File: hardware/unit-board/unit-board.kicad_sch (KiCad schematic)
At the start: 0 parts

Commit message: Add unit board schematic blocks
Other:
- added sheet CAN Interface (can_interface.kicad_sch)
- added sheet G474 Minimum (STM32G474 Minimum System.kicad_sch)
- added sheet Power Input 3.3V (power_3v3.kicad_sch)
- added sheet Power monitoring (5V monitoring.kicad_sch)
- added sheet SPI,LED,CAN_ID (amt22_spi.kicad_sch)
- title: (none) -> unit bozrd
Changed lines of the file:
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@@
 	(generator_version "10.0")
 	(paper "A4")
+	(title_block
+		(title "unit bozrd")
+		(date "2026-07-21")
+	)
+	(sheet
+		(at 142.24 21.59)
+		(size 48.26 48.26)
+		(exclude_from_sim no)
+		(in_bom yes)
+		(on_board yes)
+		(dnp no)
+		(fields_autoplaced yes)
+		(stroke
+			(width 0.1524)
+			(type solid)
+		)
+		(fill
+			(color 0 0 0 0)
+		)
+		(property "Sheetname" "G474 Minimum"
+			(at 142.24 20.8784 0)
+			(show_name no)
+			(do_not_autoplace no)
+			(effects
+				(font
+					(size 1.27 1.27)
+				)
+				(justify left bottom)
+			)
+		)
+		(property "Sheetfile" "STM32G474 Minimum System.kicad_sch"
+			(at 142.24 70.4346 0)
+			(show_name no)
+			(do_not_autoplace no)
+			(effects
+				(font
+					(size 1.27 1.27)
+				)
+				(justify left top)
+			)
+		)
+		(instances
+			(project "unit-board"
+				(path "/902d1696-b686-472b-a104-e0c03f0522c9"
+					(page "4")
+				)
+			)
+		)
+	)
+	(sheet
+		(at 81.28 21.59)
+		(size 48.26 48.26)
+		(exclude_from_sim no)
+		(in_bom yes)
+		(on_board yes)
+		(dnp no)
+		(fields_autoplaced yes)
+		(stroke
+			(width 0.1524)
+			(type solid)
+		)
+		(fill
+			(color 0 0 0 0)
+		)
+		(property "Sheetname" "CAN Interface"
+			(at 81.28 20.8784 0)
+			(show_name no)
+			(do_not_autoplace no)
+			(effects
+				(font
+					(size 1.27 1.27)
+				)
+				(justify left bottom)
+			)
+		)
+		(property "Sheetfile" "can_interface.kicad_sch"
+			(at 81.28 70.4346 0)
+			(show_name no)
+			(do_not_autoplace no)
+			(effects
+				(font
+					(size 1.27 1.27)
+				)
+				(justify left top)
+			)
+		)
+		(instances
+			(project "unit-board"
+				(path "/902d1696-b686-472b-a104-e0c03f0522c9"
+					(page "3")
+				)
+			)
+		)
+	)
+	(sheet
+		(at 207.01 21.59)
+		(size 48.26 48.26)
+		(exclude_from_sim no)
+		(in_bom yes)
+		(on_board yes)
+		(dnp no)
+		(fields_autoplaced yes)
+		(stroke
+			(width 0.1524)
+			(type solid)
+		)
+		(fill
+			(color 0 0 0 0)
+		)
+		(property "Sheetname" "SPI,LED,CAN_ID"
+			(at 207.01 20.8784 0)
+			(show_name no)
+			(do_not_autoplace no)
+			(effects
+				(font
+					(size 1.27 1.27)
+				)
+				(justify left bottom)
+			)
+		)
+		(property "Sheetfile" "amt22_spi.kicad_sch"
+			(at 207.01 70.4346 0)
+			(show_name no)
+			(do_not_autoplace no)
+			(effects
+				(font
+					(size 1.27 1.27)
+				)
+				(justify left top)
+			)
+		)
+		(instances
+			(project "unit-board"
+				(path "/902d1696-b686-472b-a104-e0c03f0522c9"
+					(page "5")
+				)
+			)
+		)
+	)
+	(sheet
+		(at 25.4 87.63)
+		(size 45.72 48.26)
+		(exclude_from_sim no)
+		(in_bom yes)
+		(on_board yes)
+		(dnp no)
+		(fields_autoplaced yes)
+		(stroke
+			(width 0.1524)
+			(type solid)
+		)
+		(fill
+			(color 0 0 0 0)
+		)
+		(property "Sheetname" "Power monitoring"
+			(at 25.4 86.9184 0)
+			(show_name no)
+			(do_not_autoplace no)
+			(effects
+				(font
+					(size 1.27 1.27)
+				)
+				(justify left bottom)
+			)
+		)
+		(property "Sheetfile" "5V monitoring.kicad_sch"
+			(at 25.4 136.4746 0)
+			(show_name no)
+			(do_not_autoplace no)
+			(effects
+				(font
+					(size 1.27 1.27)
+				)
+				(justify left top)
+			)
+		)
+		(instances
+			(project "unit-board"
+				(path "/902d1696-b686-472b-a104-e0c03f0522c9"
+					(page "6")
+				)
+			)
+		)
+	)
+	(sheet
+		(at 24.13 21.59)
+		(size 45.72 48.26)
+		(exclude_from_sim no)
+		(in_bom yes)
+		(on_board yes)
+		(dnp no)
+		(fields_autoplaced yes)
+		(stroke
+			(width 0.1524)
+			(type solid)
+		)
+		(fill
+			(color 0 0 0 0)
+		)
+		(property "Sheetname" "Power Input 3.3V"
+			(at 24.13 20.8784 0)
+			(show_name no)
+			(do_not_autoplace no)
+			(effects
+				(font
+					(size 1.27 1.27)
+				)
+				(justify left bottom)
+			)
+		)
+		(property "Sheetfile" "power_3v3.kicad_sch"
+			(at 24.13 70.4346 0)
+			(show_name no)
+			(do_not_autoplace no)
+			(effects
+				(font
+					(size 1.27 1.27)
+				)
+				(justify left top)
+			)
+		)
+		(instances
+			(project "unit-board"
+				(path "/902d1696-b686-472b-a104-e0c03f0522c9"
+					(page "2")
+				)
+			)
+		)
+	)
 	(sheet_instances
 		(path "/"

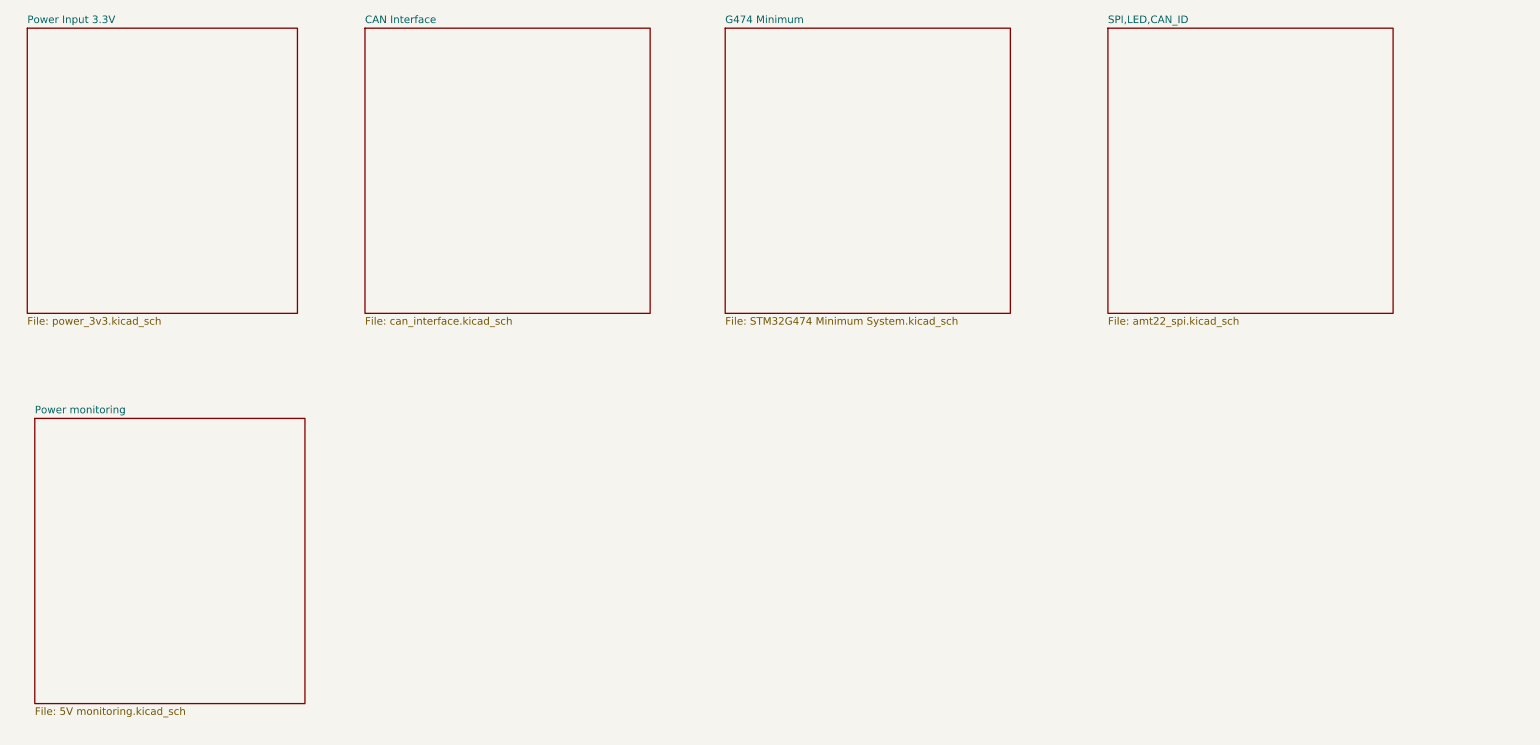
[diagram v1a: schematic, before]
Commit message: fix(hardware): resolve unit board ERC violations
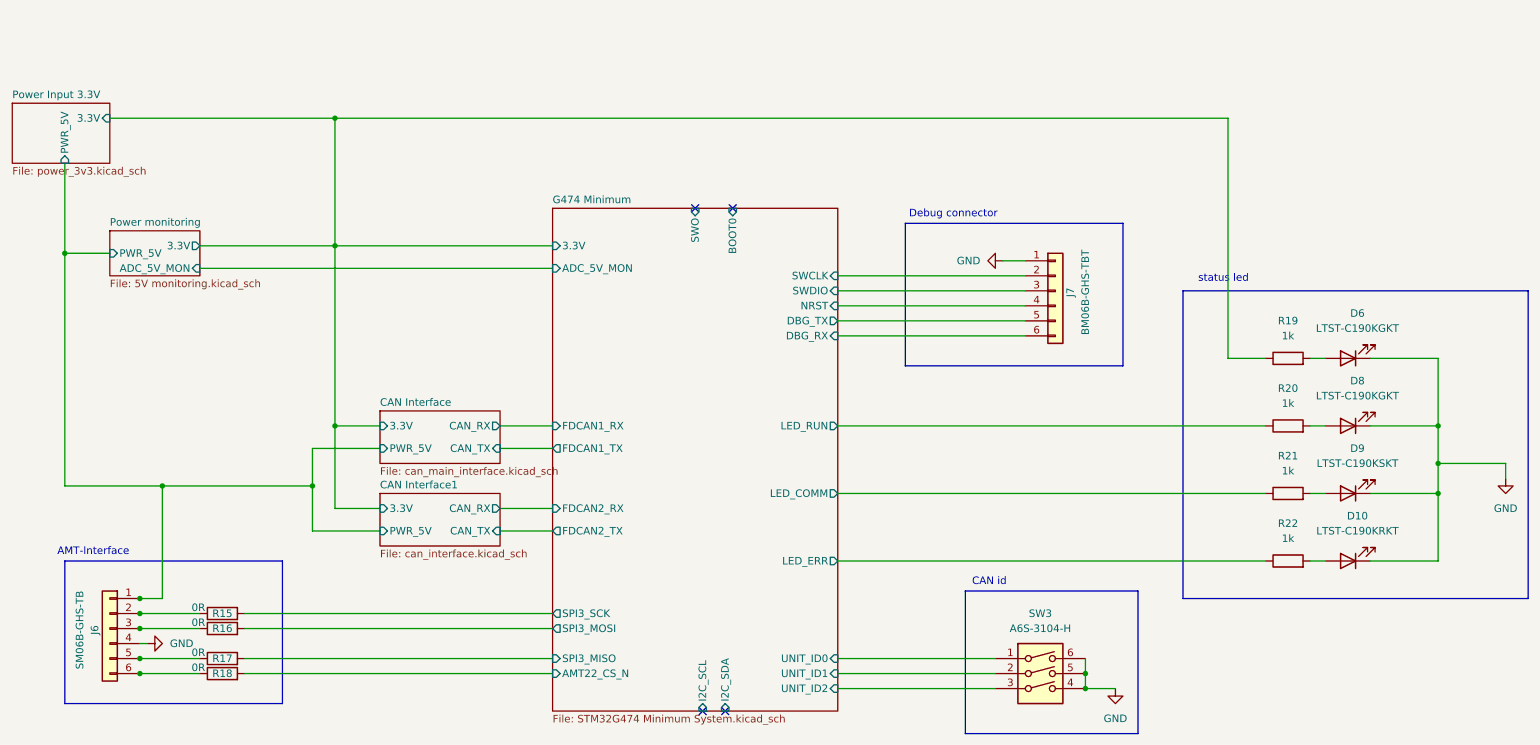
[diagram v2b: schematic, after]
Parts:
- added D10: LTST-C190KRKT, LED_SMD:LED_0603_1608Metric, symbol Device:LED
- added D6, D8: LTST-C190KGKT, LED_SMD:LED_0603_1608Metric, symbol Device:LED
- added D9: LTST-C190KSKT, LED_SMD:LED_0603_1608Metric, symbol Device:LED
- added J6: SM06B-GHS-TB, Connector_JST:JST_GH_SM06B-GHS-TB_1x06-1MP_P1.25mm_Horizontal, symbol Connector_Generic:Conn_01x06
- added J7: BM06B-GHS-TBT, Connector_JST:JST_GH_BM06B-GHS-TBT_1x06-1MP_P1.25mm_Vertical, symbol Connector_Generic:Conn_01x06
- added R15, R16, R17, R18: 0R, Resistor_SMD:R_0603_1608Metric, symbol Device:R
- added R19, R20, R21, R22: 1k, Resistor_SMD:R_0603_1608Metric, symbol Device:R
- added SW3: A6S-3104-H, Button_Switch_SMD:SW_DIP_SPSTx03_Slide_Omron_A6S-310x_W8.9mm_P2.54mm, symbol Switch:SW_DIP_x03
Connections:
- new net: J6.2 (Pin_2), R15.1
- new net: D8.2 (A), R20.2
- new net: J6.6 (Pin_6), R18.1
- new net: D6.2 (A), R19.2
- new net: D9.2 (A), R21.2
- new net: J6.3 (Pin_3), R16.1
- new net: J6.5 (Pin_5), R17.1
- new net: D10.2 (A), R22.2
- new net CAN Interface/3.3V: R19.1
- new net CAN Interface/PWR_5V: J6.1 (Pin_1)
- new net G474 Minimum/AMT22_CS_N: R18.2
- new net G474 Minimum/DBG_RX: J7.6 (Pin_6)
- new net G474 Minimum/DBG_TX: J7.5 (Pin_5)
- new net G474 Minimum/LED_COMM: R21.1
- new net G474 Minimum/LED_ERR: R22.1
- new net G474 Minimum/LED_RUN: R20.1
- new net G474 Minimum/NRST: J7.4 (Pin_4)
- new net G474 Minimum/SPI3_MISO: R17.2
- new net G474 Minimum/SPI3_MOSI: R16.2
- new net G474 Minimum/SPI3_SCK: R15.2
- new net G474 Minimum/SWCLK: J7.2 (Pin_2)
- new net G474 Minimum/SWDIO: J7.3 (Pin_3)
- new net G474 Minimum/UNIT_ID0: SW3.1
- new net G474 Minimum/UNIT_ID1: SW3.2
- new net G474 Minimum/UNIT_ID2: SW3.3
- new net GND: D10.1 (K), D6.1 (K), D8.1 (K), D9.1 (K), J6.4 (Pin_4), J7.1 (Pin_1), SW3.4, SW3.5, SW3.6
- no-connect marks 0 -> 4
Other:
- removed sheet SPI,LED,CAN_ID
- added sheet CAN Interface1 (can_interface.kicad_sch)
- sheet CAN Interface: file can_interface.kicad_sch -> can_main_interface.kicad_sch
- sheet CAN Interface ports: added 3.3V, CAN_RX, CAN_TX, PWR_5V; removed none
- sheet G474 Minimum ports: added 3.3V, ADC_5V_MON, AMT22_CS_N, BOOT0, DBG_RX, DBG_TX, FDCAN1_RX, FDCAN1_TX, FDCAN2_RX, FDCAN2_TX, I2C_SCL, I2C_SDA, LED_COMM, LED_ERR, LED_RUN, NRST, SPI3_MISO, SPI3_MOSI, SPI3_SCK, SWCLK, SWDIO, SWO, UNIT_ID0, UNIT_ID1, UNIT_ID2; removed none
- sheet Power Input 3.3V ports: added 3.3V, PWR_5V; removed none
- sheet Power monitoring ports: added 3.3V, ADC_5V_MON, PWR_5V; removed none
- note added: "AMT-Interface"
- note added: "CAN id"
- note added: "Debug connector"
- note added: "status led"
- title: unit bozrd -> unit board

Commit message: chore(hardware): update unit board design
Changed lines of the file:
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@@
 	(paper "A4")
 	(title_block
-	(title "unit board")
+		(title "unit board")
 		(date "2026-07-21")
 	)
@@
 	)
 	(junction
-		(at 43.18 120.65)
-		(diameter 0)
-		(color 0 0 0 0)
-	)
-	(junction
 		(at 262.89 88.9)
-		(diameter 0)
-		(color 0 0 0 0)
-	)
-	(junction
-		(at 43.18 130.81)
 		(diameter 0)
 		(color 0 0 0 0)
@@
 	)
 	(junction
-		(at 43.18 123.19)
-		(diameter 0)
-		(color 0 0 0 0)
-	)
-	(junction
-		(at 43.18 128.27)
-		(diameter 0)
-		(color 0 0 0 0)
-	)
-	(junction
 		(at 76.2 36.83)
 		(diameter 0)
@@
 		(diameter 0)
 		(color 0 0 0 0)
-	)
-	(junction
-		(at 43.18 118.11)
-		(diameter 0)
-		(color 0 0 0 0)
